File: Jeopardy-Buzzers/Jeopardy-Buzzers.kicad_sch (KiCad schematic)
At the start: 13 parts, among them J1 USB_C_Receptacle, U1 CH32V003FxUx, U2 CH340N, U3 NRF24L01_Breakout, U4 TPD2EUSB30, U5 AMS1117-3.3

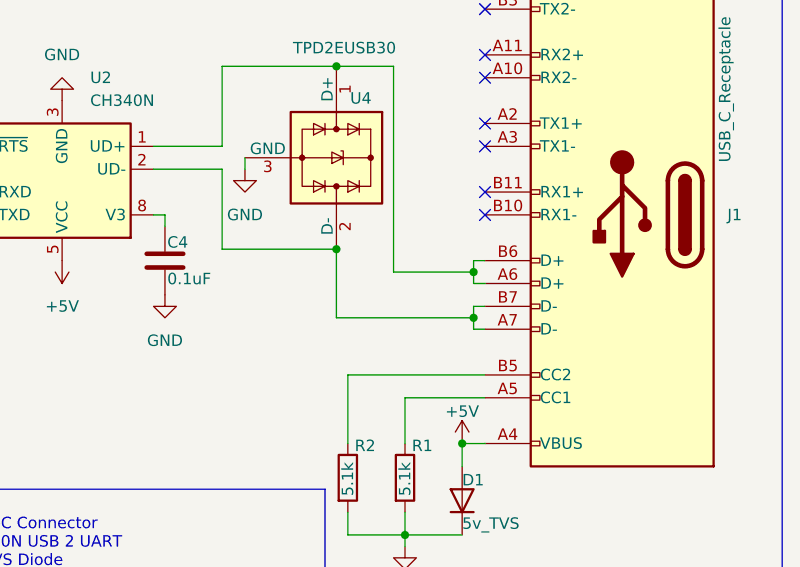
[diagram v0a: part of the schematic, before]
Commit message: Added components to the schematic & added footprints to items
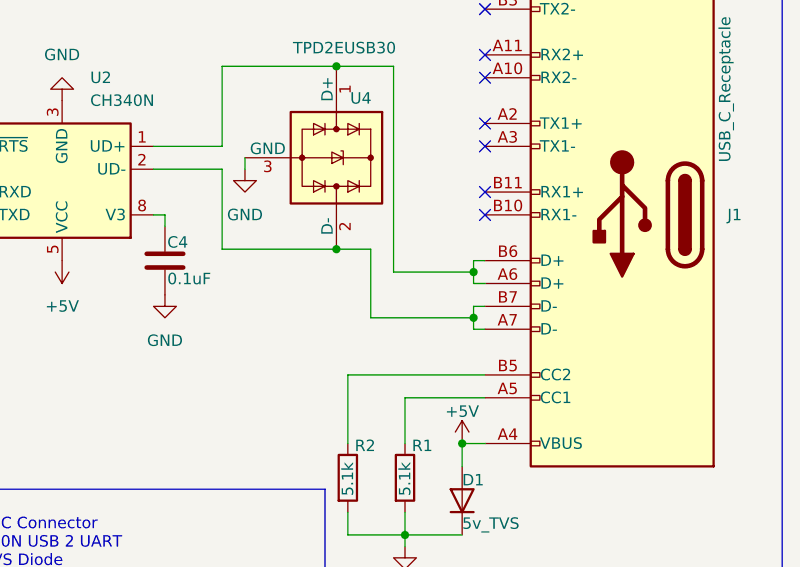
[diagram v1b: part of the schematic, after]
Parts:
- C1, C2, C3, C4, R1, R2: footprint (none) -> Resistor_SMD:R_0805_2012Metric
- D1: footprint (none) -> Diode_SMD:D_SMB
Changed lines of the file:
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@@
+	(wire
+		(pts
+			(xy 237.49 67.31) (xy 233.68 67.31)
+		)
+		(stroke
+			(width 0)
+			(type default)
+		)
+	)
 	(wire
 		(pts
@@
 	(wire
 		(pts
-			(xy 233.68 67.31) (xy 233.68 74.93)
+			(xy 237.49 67.31) (xy 237.49 74.93)
 		)
 		(stroke
@@
 	(wire
 		(pts
-			(xy 233.68 74.93) (xy 248.92 74.93)
+			(xy 237.49 74.93) (xy 248.92 74.93)
 		)
 		(stroke
@@
 			)
 		)
-		(property "Footprint" ""
+		(property "Footprint" "Resistor_SMD:R_0805_2012Metric"
 			(at 58.1152 49.53 0)
 			(effects
@@
 			)
 		)
-		(property "Footprint" ""
+		(property "Footprint" "Resistor_SMD:R_0805_2012Metric"
 			(at 53.0352 92.71 0)
 			(effects
@@
 			)
 		)
-		(property "Footprint" ""
+		(property "Footprint" "Resistor_SMD:R_0805_2012Metric"
 			(at 215.5952 72.39 0)
 			(effects
@@
 			)
 		)
-		(property "Footprint" ""
+		(property "Footprint" "Resistor_SMD:R_0805_2012Metric"
 			(at 239.522 92.71 90)
 			(effects
@@
 			)
 		)
-		(property "Footprint" ""
+		(property "Footprint" "Resistor_SMD:R_0805_2012Metric"
 			(at 32.7152 92.71 0)
 			(effects
@@
 			)
 		)
-		(property "Footprint" ""
+		(property "Footprint" "Diode_SMD:D_SMB"
 			(at 247.65 95.25 0)
 			(effects
@@
 			)
 		)
-		(property "Footprint" ""
+		(property "Footprint" "Resistor_SMD:R_0805_2012Metric"
 			(at 233.172 92.71 90)
 			(effects
